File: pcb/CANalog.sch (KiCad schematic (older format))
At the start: 82 parts, among them J1 PWR, J4 STM_PROG, J5 ESP_PROG, J6 AOUT, J7 CAN, Q1 DMP3099L-7, SW1 RESET, SW2 ESP_PROG, U1 BL9342, U2 MIC5504-3.3YM5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

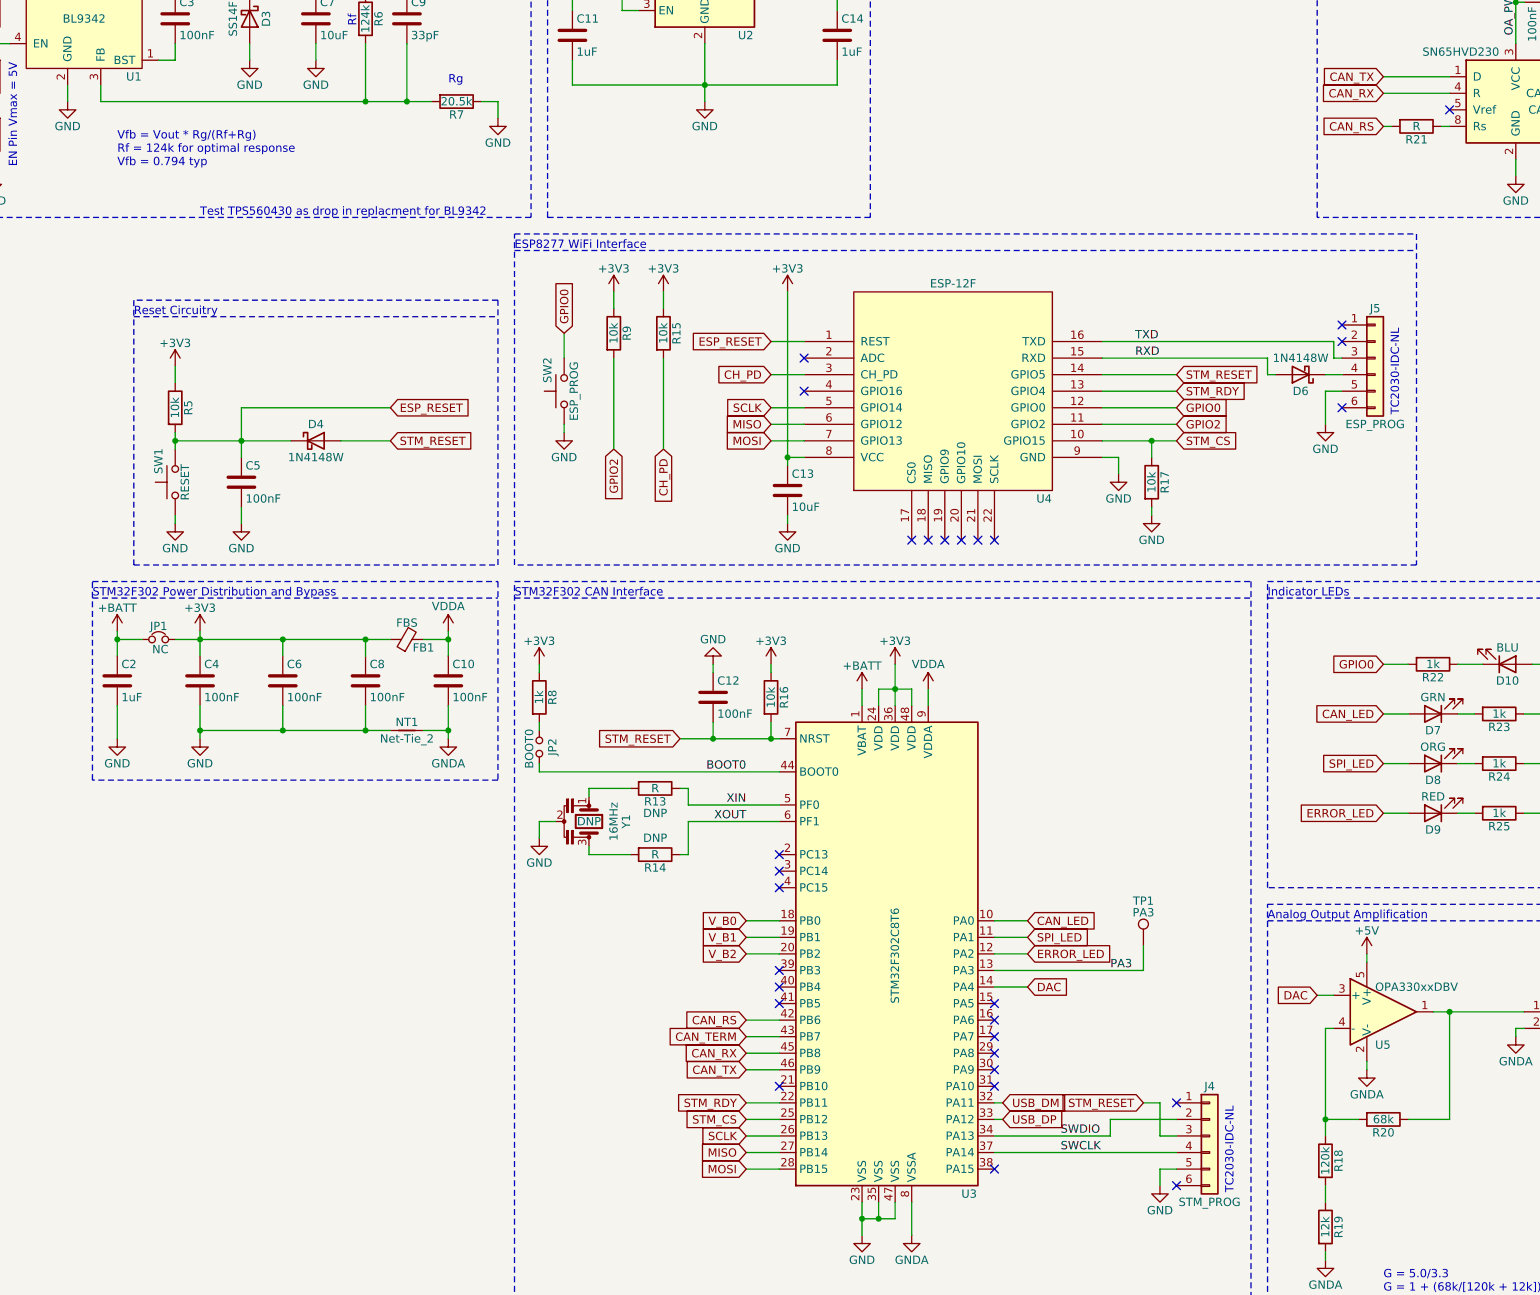
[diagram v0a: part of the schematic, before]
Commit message: remove can_rs connection to stm32
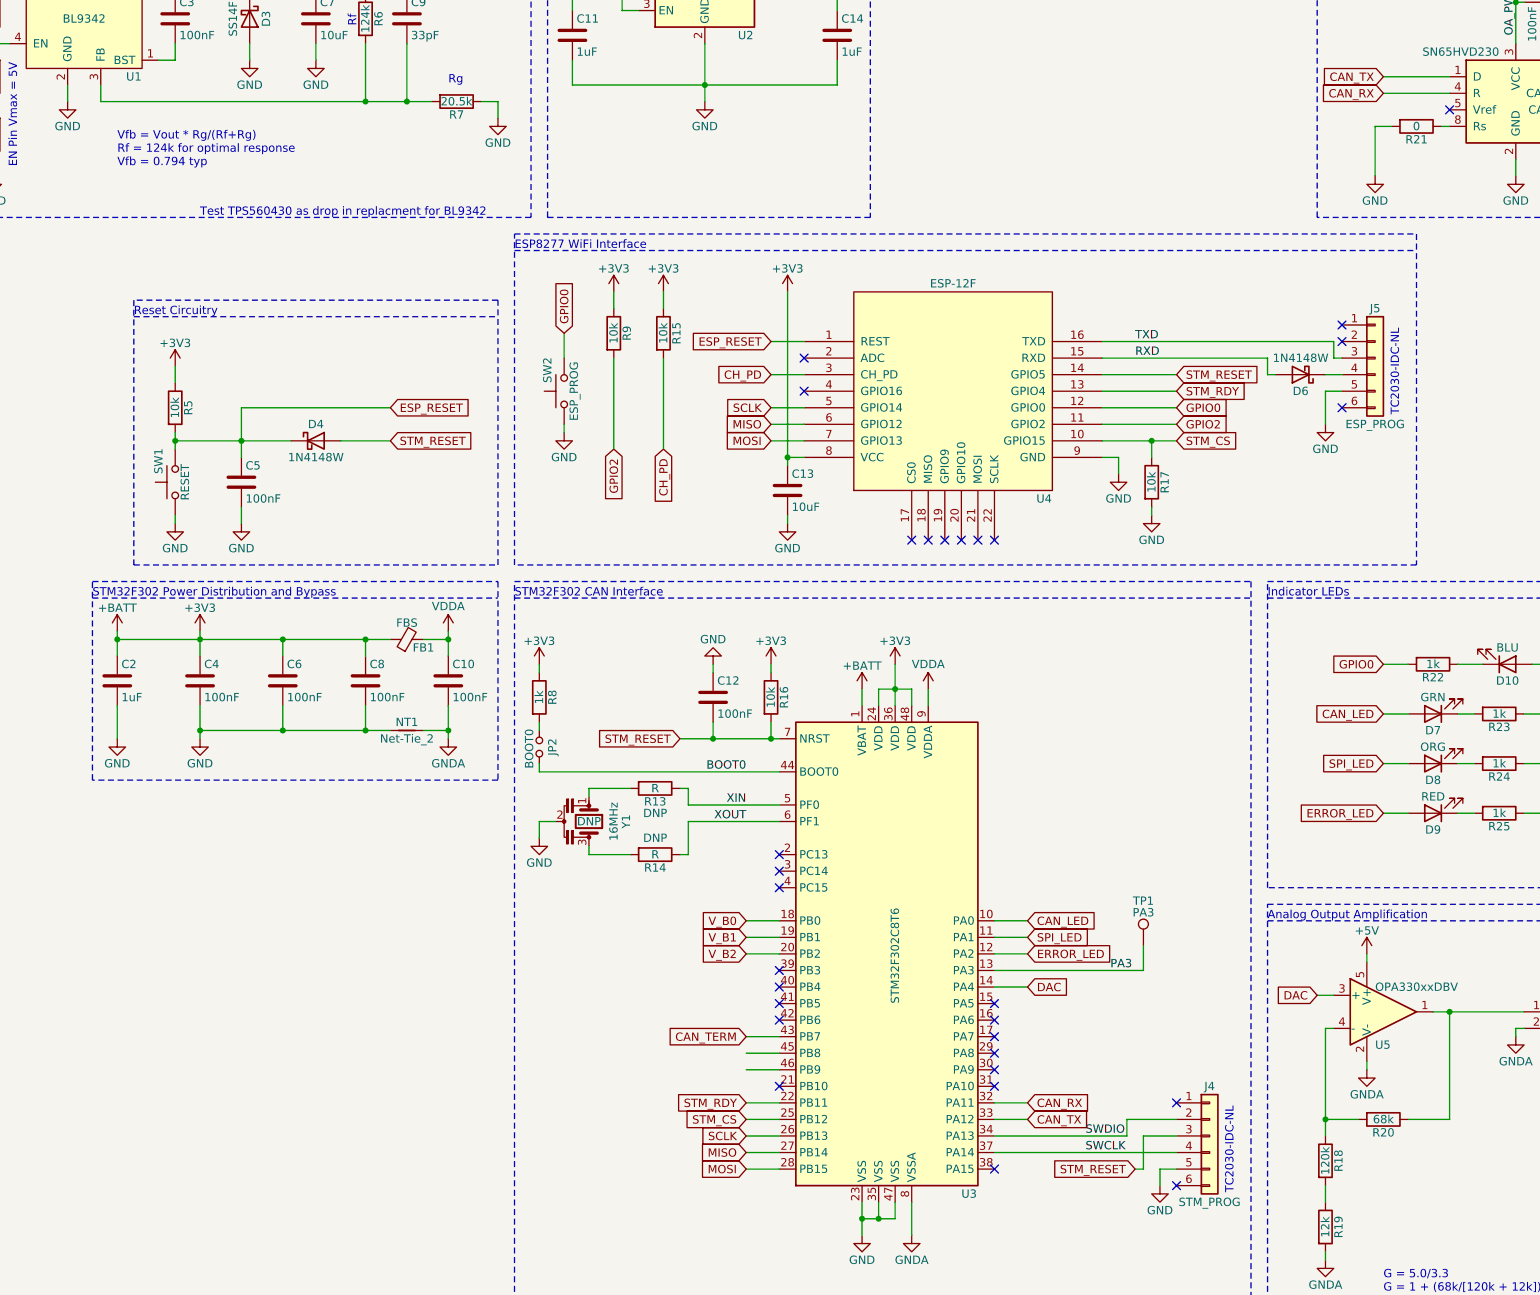
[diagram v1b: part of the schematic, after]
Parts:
- removed JP1: NC, Jumper:SolderJumper-2_P1.3mm_Bridged_RoundedPad1.0x1.5mm, symbol Device:Jumper_NC_Small
- R21: value R -> 0
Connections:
- net +BATT is gone; now on net +3V3: C2.1, U3.1 (VBAT)
- net USB_DM is gone; now on net CAN_RX: U3.32 (PA11)
- net USB_DP is gone; now on net CAN_TX: U3.33 (PA12)
- net CAN_RX: no longer U3.45 (PB8)
- net CAN_TX: no longer U3.46 (PB9)
- net GND: now also R21.2
- net CAN_RS: no longer names the net of U3.42 (PB6)
- net CAN_RS: no longer R21.2
- no-connect marks 28 -> 29
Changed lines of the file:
@@
 	1    0    0    -1
 $EndComp
-Connection ~ 3800 5100
-Wire Wire Line
-	3800 5100 3800 5200
-Wire Wire Line
-	3800 5100 3800 5050
-Wire Wire Line
-	3950 5100 3800 5100
-Wire Wire Line
-	4150 5100 4300 5100
+Wire Wire Line
+	3800 5100 4300 5100
 $Comp
 L Device:C C2
@@
 F 8 "https://www.digikey.com/en/products/detail/samsung-electro-mechanics/CL10A105KQ8NNNC/3886694?s=N4IgTCBcDaIIxgOwDYC0cAMBmNdUDsATEAXQF8g" H 3800 5350 50  0001 C CNN "Supplier Link"
 	1    3800 5350
-	1    0    0    -1
-$EndComp
-$Comp
-L Device:Jumper_NC_Small JP1
-U 1 1 613708F8
-P 4050 5100
-F 0 "JP1" H 4050 5180 50  0000 C CNN
-F 1 "NC" H 4060 5040 50  0000 C CNN
-F 2 "Jumper:SolderJumper-2_P1.3mm_Bridged_RoundedPad1.0x1.5mm" H 4050 5100 50  0001 C CNN
-F 3 "~" H 4050 5100 50  0001 C CNN
-F 4 "DNP" H 4050 5100 50  0001 C CNN "Population"
-	1    4050 5100
 	1    0    0    -1
 $EndComp
@@
 Wire Wire Line
 	10100 8400 10100 8300
-Text Label 9500 8200 0    50   ~ 0
+Text Label 9650 8200 0    50   ~ 0
 SWCLK
-Text Label 9500 8100 0    50   ~ 0
+Text Label 9650 8100 0    50   ~ 0
 SWDIO
 $Comp
@@
 Text GLabel 9300 7200 2    50   Input ~ 0
 DAC
-Text GLabel 7600 7600 0    50   Input ~ 0
+Text GLabel 9300 7900 2    50   Input ~ 0
 CAN_RX
-Text GLabel 7600 7700 0    50   Input ~ 0
+Text GLabel 9300 8000 2    50   Input ~ 0
 CAN_TX
 Wire Wire Line
@@
 Wire Wire Line
 	7800 8300 7600 8300
-Wire Wire Line
-	9100 7900 9150 7900
-Wire Wire Line
-	9100 8000 9150 8000
 Text GLabel 7600 8000 0    50   Input ~ 0
 STM_CS
@@
 Wire Wire Line
 	7600 7500 7800 7500
-Text GLabel 7600 7400 0    50   Input ~ 0
-CAN_RS
-Wire Wire Line
-	7600 7400 7800 7400
 $Comp
 L power:GND #PWR039
@@
 P 11650 2000
 F 0 "R21" V 11730 2000 50  0000 C CNN
-F 1 "R" V 11650 2000 50  0000 C CNN
+F 1 "0" V 11650 2000 50  0000 C CNN
 F 2 "Resistor_SMD:R_0603_1608Metric" V 11580 2000 50  0001 C CNN
 F 3 "~" H 11650 2000 50  0001 C CNN
@@
 	1    0    0    -1
 $EndComp
-Text GLabel 11450 2000 0    50   Input ~ 0
-CAN_RS
-Wire Wire Line
-	11500 2000 11450 2000
 Wire Wire Line
 	11800 2000 11850 2000
@@
 NoConn ~ 10200 7900
 Wire Wire Line
-	9100 8100 9800 8100
-Wire Wire Line
-	9800 8100 9800 8000
-Wire Wire Line
-	9800 8000 10200 8000
+	9100 8100 9900 8100
+Wire Wire Line
+	9900 8100 9900 8000
+Wire Wire Line
+	9900 8000 10200 8000
 NoConn ~ 10200 8400
-Text GLabel 9150 8000 2    50   Input ~ 0
-USB_DP
-Text GLabel 9150 7900 2    50   Input ~ 0
-USB_DM
-Text GLabel 10000 7900 0    50   Input ~ 0
+Text GLabel 9950 8300 0    50   Input ~ 0
 STM_RESET
 Wire Wire Line
-	10000 7900 10100 7900
-Wire Wire Line
-	10100 7900 10100 8100
-Wire Wire Line
-	10100 8100 10200 8100
+	3800 5050 3800 5100
+Connection ~ 3800 5100
+Wire Wire Line
+	3800 5100 3800 5200
+$Comp
+L power:GND #PWR?
+U 1 1 60908C01
+P 11400 2300
+F 0 "#PWR?" H 11400 2050 50  0001 C CNN
+F 1 "GND" H 11400 2150 50  0000 C CNN
+F 2 "" H 11400 2300 50  0001 C CNN
+F 3 "" H 11400 2300 50  0001 C CNN
+	1    11400 2300
+	1    0    0    -1
+$EndComp
+Wire Wire Line
+	11400 2300 11400 2000
+Wire Wire Line
+	11400 2000 11500 2000
+NoConn ~ 7800 7400
+Wire Wire Line
+	10200 8100 10000 8100
+Wire Wire Line
+	10000 8100 10000 8300
+Wire Wire Line
+	10000 8300 9950 8300
+Wire Wire Line
+	9300 7900 9100 7900
+Wire Wire Line
+	9300 8000 9100 8000
 $EndSCHEMATC

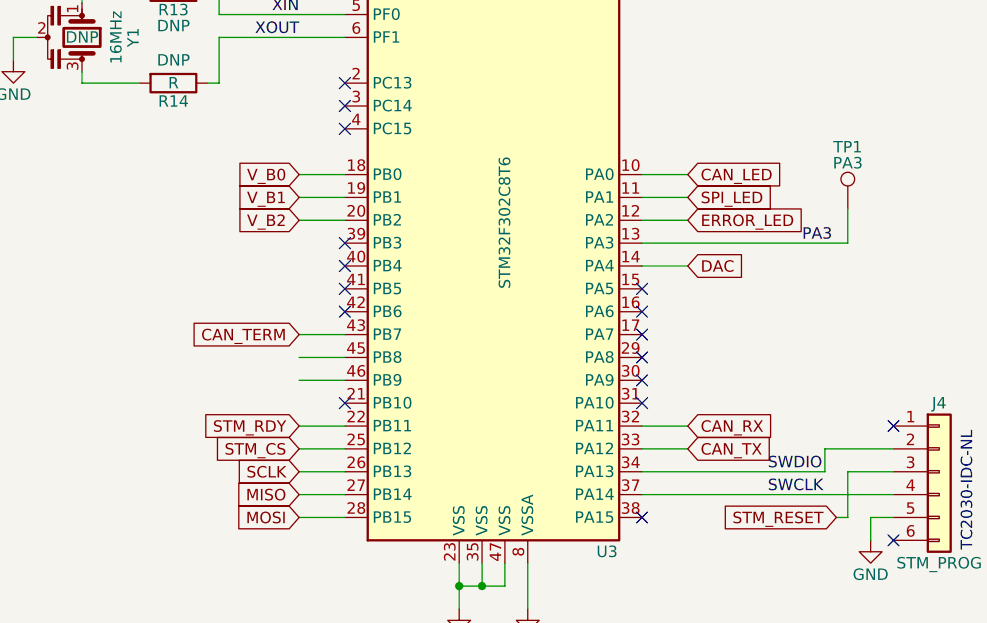
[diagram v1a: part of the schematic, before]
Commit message: stm32 pin swaping
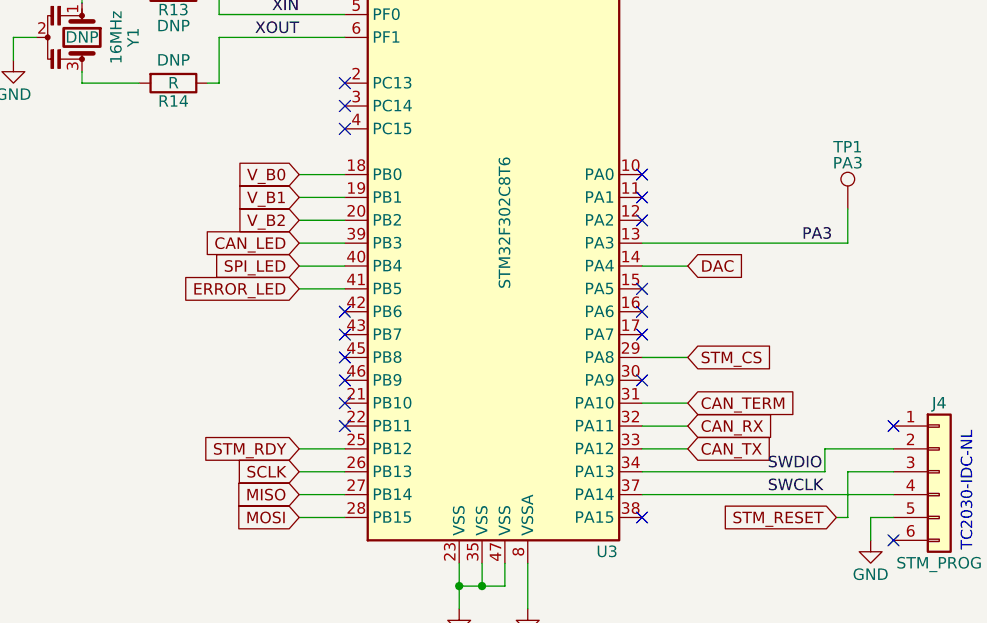
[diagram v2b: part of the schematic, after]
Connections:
- net CAN_LED: now also U3.39 (PB3); no longer U3.10 (PA0)
- net CAN_TERM: now also U3.31 (PA10); no longer U3.43 (PB7)
- net ERROR_LED: now also U3.41 (PB5); no longer U3.12 (PA2)
- net SPI_LED: now also U3.40 (PB4); no longer U3.11 (PA1)
- net STM_CS: now also U3.29 (PA8); no longer U3.25 (PB12)
- net STM_RDY: now also U3.25 (PB12); no longer U3.22 (PB11)
- no-connect marks 29 -> 31
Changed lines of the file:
@@
 	1    0    0    -1
 $EndComp
-NoConn ~ 9100 7600
 Wire Wire Line
 	10100 8300 10200 8300
@@
 Text GLabel 9300 8000 2    50   Input ~ 0
 CAN_TX
-Wire Wire Line
-	7800 7600 7600 7600
-Wire Wire Line
-	7800 7700 7600 7700
 Text GLabel 7600 8100 0    50   Input ~ 0
 SCLK
@@
 Wire Wire Line
 	7800 8300 7600 8300
+Text GLabel 9300 7600 2    50   Input ~ 0
+STM_CS
+Wire Wire Line
+	7600 8000 7800 8000
 Text GLabel 7600 8000 0    50   Input ~ 0
-STM_CS
-Wire Wire Line
-	7600 8000 7800 8000
-Text GLabel 7600 7900 0    50   Input ~ 0
 STM_RDY
-Wire Wire Line
-	7600 7900 7800 7900
 $Comp
 L Device:Resonator Y1
@@
 	1    0    0    -1
 $EndComp
-Text GLabel 7600 7500 0    50   Input ~ 0
+Text GLabel 9300 7800 2    50   Input ~ 0
 CAN_TERM
-Wire Wire Line
-	7600 7500 7800 7500
 $Comp
 L power:GND #PWR039
@@
 Wire Notes Line
 	10650 4750 10650 9100
-Text GLabel 9300 6800 2    50   Input ~ 0
+Text GLabel 7600 7100 0    50   Input ~ 0
 CAN_LED
-Text GLabel 9300 6900 2    50   Input ~ 0
+Text GLabel 7600 7200 0    50   Input ~ 0
 SPI_LED
-Text GLabel 9300 7000 2    50   Input ~ 0
+Text GLabel 7600 7300 0    50   Input ~ 0
 ERROR_LED
-Wire Wire Line
-	9100 6800 9300 6800
-Wire Wire Line
-	9100 6900 9300 6900
-Wire Wire Line
-	9100 7000 9300 7000
 $Comp
 L Connector_Generic:Conn_01x03 J7
@@
 Wire Wire Line
 	6000 1100 6550 1100
-NoConn ~ 7800 7100
-NoConn ~ 7800 7200
-NoConn ~ 7800 7300
 NoConn ~ 9100 7700
-NoConn ~ 9100 7800
 NoConn ~ 9100 8300
 Wire Wire Line
@@
 Wire Wire Line
 	9300 8000 9100 8000
+NoConn ~ 7800 7600
+NoConn ~ 7800 7700
+Wire Wire Line
+	9100 7800 9300 7800
+NoConn ~ 7800 7500
+NoConn ~ 7800 7900
+Wire Wire Line
+	9100 7600 9300 7600
+Wire Wire Line
+	7600 7100 7800 7100
+Wire Wire Line
+	7600 7200 7800 7200
+Wire Wire Line
+	7600 7300 7800 7300
+NoConn ~ 9100 6800
+NoConn ~ 9100 6900
+NoConn ~ 9100 7000
 $EndSCHEMATC

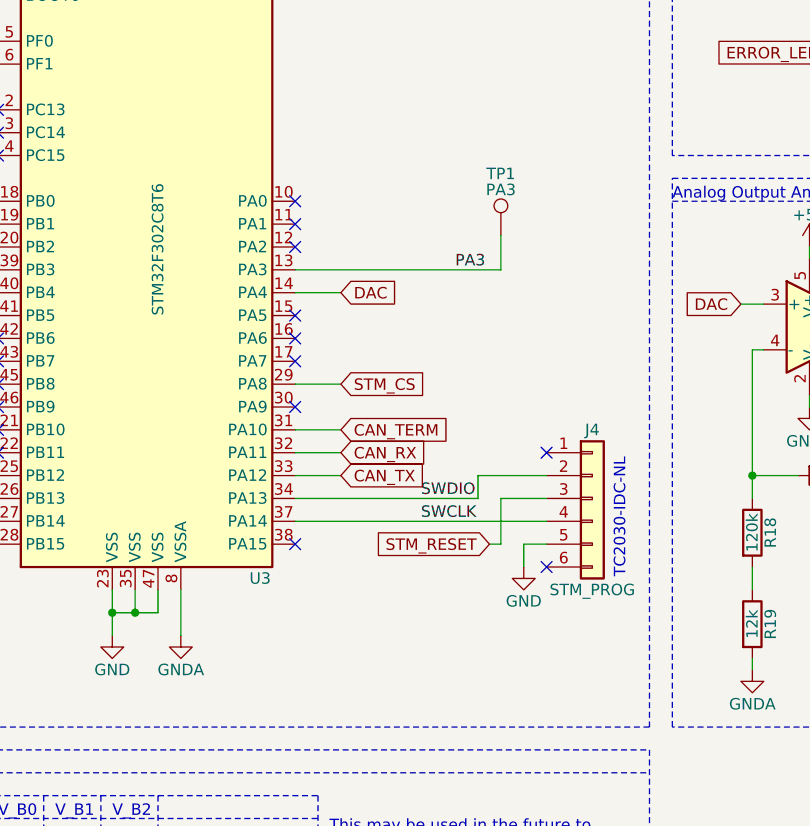
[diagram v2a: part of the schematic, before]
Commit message: move tp to pa15
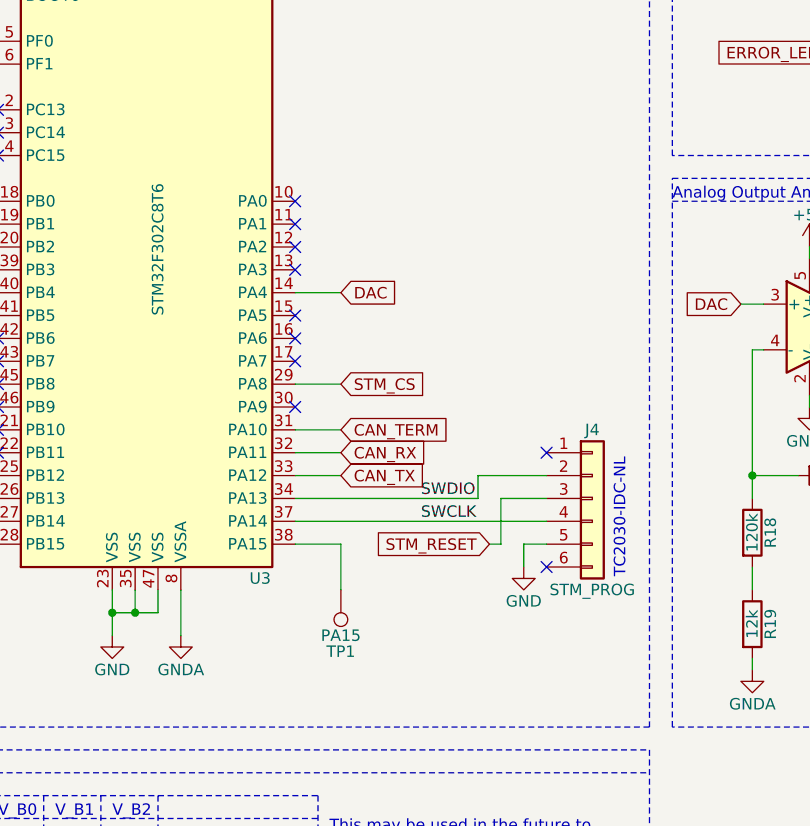
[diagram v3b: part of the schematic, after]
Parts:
- TP1: value PA3 -> PA15
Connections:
- net at U3.38 (PA15): now also TP1.1
- net PA3: no longer names the net of U3.13 (PA3)
- net PA3: no longer TP1.1
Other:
- moved on the sheet: TP1
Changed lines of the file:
@@
 Wire Wire Line
 	6350 5900 7800 5900
-Text Label 9800 7100 0    50   ~ 0
-PA3
 NoConn ~ 7800 6400
 NoConn ~ 7800 6600
@@
 L Connector:TestPoint TP1
 U 1 1 60D0AAE6
-P 10000 6950
-F 0 "TP1" H 10000 7220 50  0000 C CNN
-F 1 "PA3" H 10000 7150 50  0000 C CNN
-F 2 "TestPoint:TestPoint_Pad_D1.0mm" H 10200 6950 50  0001 C CNN
-F 3 "~" H 10200 6950 50  0001 C CNN
-	1    10000 6950
-	1    0    0    -1
+P 9300 8500
+F 0 "TP1" H 9300 8770 50  0000 C CNN
+F 1 "PA15" H 9300 8700 50  0000 C CNN
+F 2 "TestPoint:TestPoint_Pad_D1.0mm" H 9500 8500 50  0001 C CNN
+F 3 "~" H 9500 8500 50  0001 C CNN
+	1    9300 8500
+	-1   0    0    1
 $EndComp
 Wire Wire Line
@@
 	6000 1100 6550 1100
 NoConn ~ 9100 7700
-NoConn ~ 9100 8300
-Wire Wire Line
-	10000 7100 10000 6950
-Wire Wire Line
-	10000 7100 9100 7100
 Wire Wire Line
 	11100 3800 11100 3600
@@
 	3800 5100 3800 5200
 $Comp
-L power:GND #PWR?
+L power:GND #PWR0101
 U 1 1 60908C01
 P 11400 2300
-F 0 "#PWR?" H 11400 2050 50  0001 C CNN
+F 0 "#PWR0101" H 11400 2050 50  0001 C CNN
 F 1 "GND" H 11400 2150 50  0000 C CNN
 F 2 "" H 11400 2300 50  0001 C CNN
@@
 NoConn ~ 9100 6900
 NoConn ~ 9100 7000
+NoConn ~ 9100 7100
+Wire Wire Line
+	9100 8300 9300 8300
+Wire Wire Line
+	9300 8300 9300 8500
 $EndSCHEMATC
